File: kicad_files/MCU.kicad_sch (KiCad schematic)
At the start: 24 parts, among them SW1 SW_Push, SW2 SW_Push, U1 STM32F407VGTx, Y1 LFXTAL036869Reel 8MHz Crystal

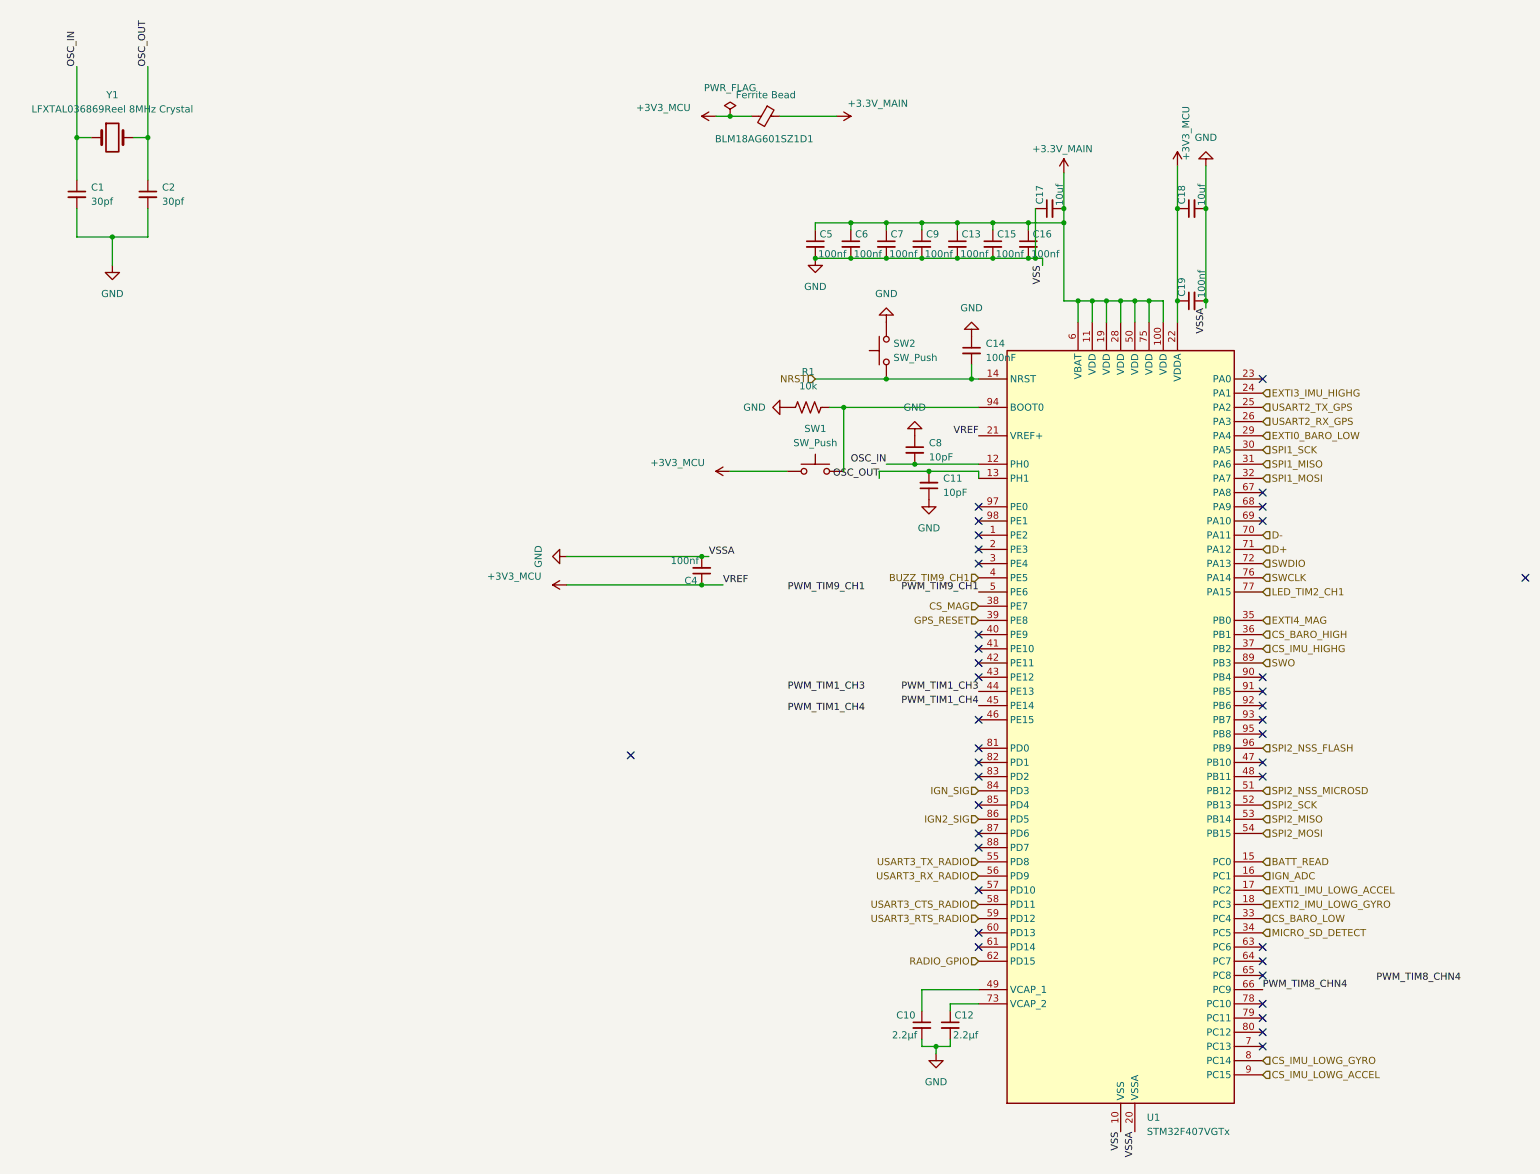
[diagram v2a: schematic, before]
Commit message: add dedicated power switching
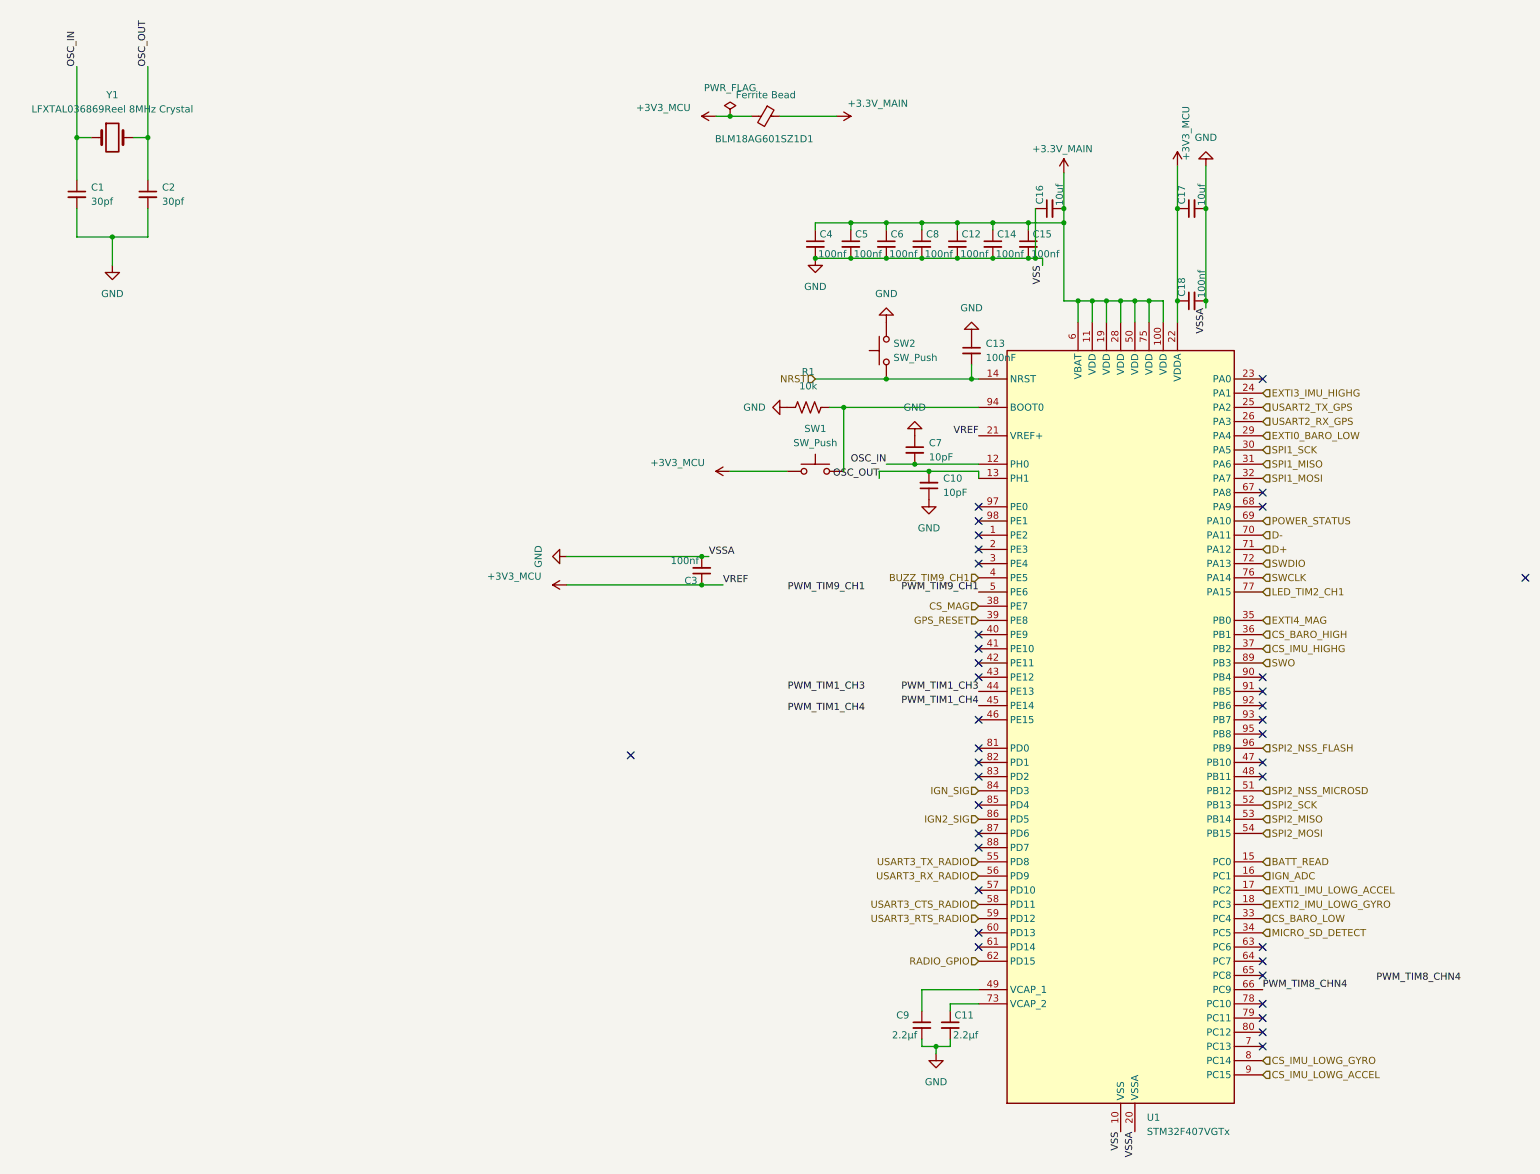
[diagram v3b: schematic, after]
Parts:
- renumbered C11 to C10, C12 to C11, C13 to C12, C14 to C13, C15 to C14, C16 to C15, C17 to C16, C18 to C17, C19 to C18, C4 to C3, C5 to C4, C6 to C5, C7 to C6, C8 to C7, C9 to C8, C10 to C9
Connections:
- net POWER_STATUS: now reaches U1.69 (PA10)
- no-connect marks 39 -> 38
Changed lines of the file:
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@@
 	)
 	(no_connect
-		(at 250.19 119.38)
-	)
-	(no_connect
 		(at 250.19 157.48)
 	)
@@
 		)
 	)
+	(hierarchical_label "POWER_STATUS"
+		(shape input)
+		(at 250.19 119.38 0)
+		(effects
+			(font
+				(size 1.27 1.27)
+			)
+			(justify left)
+		)
+	)
 	(hierarchical_label "CS_IMU_LOWG_GYRO"
 		(shape input)
@@
 		(in_pos_files yes)
 		(dnp no)
-		(property "Reference" "C16"
+		(property "Reference" "C15"
 			(at 209.042 68.072 0)
 			(show_name no)
@@
 			(project "versorlite"
 				(path "/1a230af0-0a74-48f7-8607-b087121dda49/a6e36be3-aff5-4566-a903-d81edfd88a96"
-					(reference "C16")
+					(reference "C15")
 					(unit 1)
 				)
@@
 		(dnp no)
 		(fields_autoplaced yes)
-		(property "Reference" "#PWR05"
+		(property "Reference" "#PWR06"
 			(at 158.75 99.06 0)
 			(hide yes)
@@
 			(project "versorlite"
 				(path "/1a230af0-0a74-48f7-8607-b087121dda49/a6e36be3-aff5-4566-a903-d81edfd88a96"
-					(reference "#PWR05")
+					(reference "#PWR06")
 					(unit 1)
 				)
@@
 		(in_pos_files yes)
 		(dnp no)
-		(property "Reference" "C9"
+		(property "Reference" "C8"
 			(at 189.992 68.072 0)
 			(show_name no)
@@
 			(project "versorlite"
 				(path "/1a230af0-0a74-48f7-8607-b087121dda49/a6e36be3-aff5-4566-a903-d81edfd88a96"
-					(reference "C9")
+					(reference "C8")
 					(unit 1)
 				)
@@
 		(in_pos_files yes)
 		(dnp no)
-		(property "Reference" "#PWR014"
+		(property "Reference" "#PWR015"
 			(at 234.95 59.69 0)
 			(hide yes)
@@
 			(project "versorlite"
 				(path "/1a230af0-0a74-48f7-8607-b087121dda49/a6e36be3-aff5-4566-a903-d81edfd88a96"
-					(reference "#PWR014")
+					(reference "#PWR015")
 					(unit 1)
 				)
@@
 		(dnp no)
 		(fields_autoplaced yes)
-		(property "Reference" "#PWR012"
+		(property "Reference" "#PWR013"
 			(at 198.12 80.01 0)
 			(hide yes)
@@
 			(project "versorlite"
 				(path "/1a230af0-0a74-48f7-8607-b087121dda49/a6e36be3-aff5-4566-a903-d81edfd88a96"
-					(reference "#PWR012")
+					(reference "#PWR013")
 					(unit 1)
 				)
@@
 		(dnp no)
 		(fields_autoplaced yes)
-		(property "Reference" "C8"
+		(property "Reference" "C7"
 			(at 190.5 105.4162 0)
 			(show_name no)
@@
 			(project "versorlite"
 				(path "/1a230af0-0a74-48f7-8607-b087121dda49/a6e36be3-aff5-4566-a903-d81edfd88a96"
-					(reference "C8")
+					(reference "C7")
 					(unit 1)
 				)
@@
 		(in_pos_files yes)
 		(dnp no)
-		(property "Reference" "C5"
+		(property "Reference" "C4"
 			(at 170.942 68.072 0)
 			(show_name no)
@@
 			(project "versorlite"
 				(path "/1a230af0-0a74-48f7-8607-b087121dda49/a6e36be3-aff5-4566-a903-d81edfd88a96"
-					(reference "C5")
+					(reference "C4")
 					(unit 1)
 				)
@@
 		(dnp no)
 		(fields_autoplaced yes)
-		(property "Reference" "C11"
+		(property "Reference" "C10"
 			(at 193.04 111.7535 0)
 			(show_name no)
@@
 			(project "versorlite"
 				(path "/1a230af0-0a74-48f7-8607-b087121dda49/a6e36be3-aff5-4566-a903-d81edfd88a96"
-					(reference "C11")
+					(reference "C10")
 					(unit 1)
 				)
@@
 		(in_pos_files yes)
 		(dnp no)
-		(property "Reference" "C4"
+		(property "Reference" "C3"
 			(at 149.098 130.048 0)
 			(show_name no)
@@
 			(project "versorlite"
 				(path "/1a230af0-0a74-48f7-8607-b087121dda49/a6e36be3-aff5-4566-a903-d81edfd88a96"
-					(reference "C4")
+					(reference "C3")
 					(unit 1)
 				)
@@
 		(in_pos_files yes)
 		(dnp no)
-		(property "Reference" "C7"
+		(property "Reference" "C6"
 			(at 183.642 68.072 0)
 			(show_name no)
@@
 			(project "versorlite"
 				(path "/1a230af0-0a74-48f7-8607-b087121dda49/a6e36be3-aff5-4566-a903-d81edfd88a96"
-					(reference "C7")
+					(reference "C6")
 					(unit 1)
 				)
@@
 		(in_pos_files yes)
 		(dnp no)
-		(property "Reference" "C10"
+		(property "Reference" "C9"
 			(at 184.658 207.772 0)
 			(show_name no)
@@
 			(project "versorlite"
 				(path "/1a230af0-0a74-48f7-8607-b087121dda49/a6e36be3-aff5-4566-a903-d81edfd88a96"
-					(reference "C10")
+					(reference "C9")
 					(unit 1)
 				)
@@
 		(in_pos_files yes)
 		(dnp no)
-		(property "Reference" "#PWR053"
+		(property "Reference" "#PWR05"
 			(at 158.75 110.49 0)
 			(hide yes)
@@
 			(project "versorlite"
 				(path "/1a230af0-0a74-48f7-8607-b087121dda49/a6e36be3-aff5-4566-a903-d81edfd88a96"
-					(reference "#PWR053")
+					(reference "#PWR05")
 					(unit 1)
 				)
@@
 		(dnp no)
 		(fields_autoplaced yes)
-		(property "Reference" "#PWR015"
+		(property "Reference" "#PWR016"
 			(at 240.03 49.53 0)
 			(hide yes)
@@
 			(project "versorlite"
 				(path "/1a230af0-0a74-48f7-8607-b087121dda49/a6e36be3-aff5-4566-a903-d81edfd88a96"
-					(reference "#PWR015")
+					(reference "#PWR016")
 					(unit 1)
 				)
@@
 		(in_pos_files yes)
 		(dnp no)
-		(property "Reference" "C18"
+		(property "Reference" "C17"
 			(at 235.712 62.738 0)
 			(show_name no)
@@
 			(project "versorlite"
 				(path "/1a230af0-0a74-48f7-8607-b087121dda49/a6e36be3-aff5-4566-a903-d81edfd88a96"
-					(reference "C18")
+					(reference "C17")
 					(unit 1)
 				)
@@
 		(dnp no)
 		(fields_autoplaced yes)
-		(property "Reference" "#PWR09"
+		(property "Reference" "#PWR010"
 			(at 187.96 97.79 0)
 			(hide yes)
@@
 			(project "versorlite"
 				(path "/1a230af0-0a74-48f7-8607-b087121dda49/a6e36be3-aff5-4566-a903-d81edfd88a96"
-					(reference "#PWR09")
+					(reference "#PWR010")
 					(unit 1)
 				)
@@
 		(in_pos_files yes)
 		(dnp no)
-		(property "Reference" "C19"
+		(property "Reference" "C18"
 			(at 235.712 79.248 0)
 			(show_name no)
@@
 			(project "versorlite"
 				(path "/1a230af0-0a74-48f7-8607-b087121dda49/a6e36be3-aff5-4566-a903-d81edfd88a96"
-					(reference "C19")
+					(reference "C18")
 					(unit 1)
 				)
@@
 		(in_pos_files yes)
 		(dnp no)
-		(property "Reference" "#PWR07"
+		(property "Reference" "#PWR08"
 			(at 170.18 46.99 0)
 			(hide yes)
@@
 			(project "versorlite"
 				(path "/1a230af0-0a74-48f7-8607-b087121dda49/a6e36be3-aff5-4566-a903-d81edfd88a96"
-					(reference "#PWR07")
+					(reference "#PWR08")
 					(unit 1)
 				)
@@
 		(in_pos_files yes)
 		(dnp no)
-		(property "Reference" "C17"
+		(property "Reference" "C16"
 			(at 210.312 62.738 0)
 			(show_name no)
@@
 			(project "versorlite"
 				(path "/1a230af0-0a74-48f7-8607-b087121dda49/a6e36be3-aff5-4566-a903-d81edfd88a96"
-					(reference "C17")
+					(reference "C16")
 					(unit 1)
 				)
@@
 		(in_pos_files yes)
 		(dnp no)
-		(property "Reference" "#PWR013"
+		(property "Reference" "#PWR014"
 			(at 214.63 60.96 0)
 			(hide yes)
@@
 			(project "versorlite"
 				(path "/1a230af0-0a74-48f7-8607-b087121dda49/a6e36be3-aff5-4566-a903-d81edfd88a96"
-					(reference "#PWR013")
+					(reference "#PWR014")
 					(unit 1)
 				)
@@
 		(in_pos_files yes)
 		(dnp no)
-		(property "Reference" "C15"
+		(property "Reference" "C14"
 			(at 202.692 68.072 0)
 			(show_name no)
@@
 			(project "versorlite"
 				(path "/1a230af0-0a74-48f7-8607-b087121dda49/a6e36be3-aff5-4566-a903-d81edfd88a96"
-					(reference "C15")
+					(reference "C14")
 					(unit 1)
 				)
@@
 		(in_pos_files yes)
 		(dnp no)
-		(property "Reference" "C12"
+		(property "Reference" "C11"
 			(at 195.072 207.772 0)
 			(show_name no)
@@
 			(project "versorlite"
 				(path "/1a230af0-0a74-48f7-8607-b087121dda49/a6e36be3-aff5-4566-a903-d81edfd88a96"
-					(reference "C12")
+					(reference "C11")
 					(unit 1)
 				)
@@
 		(dnp no)
 		(fields_autoplaced yes)
-		(property "Reference" "#PWR06"
+		(property "Reference" "#PWR07"
 			(at 170.18 78.74 0)
 			(hide yes)
@@
 			(project "versorlite"
 				(path "/1a230af0-0a74-48f7-8607-b087121dda49/a6e36be3-aff5-4566-a903-d81edfd88a96"
-					(reference "#PWR06")
+					(reference "#PWR07")
 					(unit 1)
 				)
@@
 		(in_pos_files yes)
 		(dnp no)
-		(property "Reference" "C13"
+		(property "Reference" "C12"
 			(at 196.342 68.072 0)
 			(show_name no)
@@
 			(project "versorlite"
 				(path "/1a230af0-0a74-48f7-8607-b087121dda49/a6e36be3-aff5-4566-a903-d81edfd88a96"
-					(reference "C13")
+					(reference "C12")
 					(unit 1)
 				)
@@
 		(dnp no)
 		(fields_autoplaced yes)
-		(property "Reference" "#PWR011"
+		(property "Reference" "#PWR012"
 			(at 191.77 220.98 0)
 			(hide yes)
@@
 			(project "versorlite"
 				(path "/1a230af0-0a74-48f7-8607-b087121dda49/a6e36be3-aff5-4566-a903-d81edfd88a96"
-					(reference "#PWR011")
+					(reference "#PWR012")
 					(unit 1)
 				)
@@
 		(dnp no)
 		(fields_autoplaced yes)
-		(property "Reference" "C14"
+		(property "Reference" "C13"
 			(at 200.66 87.6362 0)
 			(show_name no)
@@
 			(project "versorlite"
 				(path "/1a230af0-0a74-48f7-8607-b087121dda49/a6e36be3-aff5-4566-a903-d81edfd88a96"
-					(reference "C14")
+					(reference "C13")
 					(unit 1)
 				)
@@
 		(dnp no)
 		(fields_autoplaced yes)
-		(property "Reference" "#PWR010"
+		(property "Reference" "#PWR011"
 			(at 190.5 121.92 0)
 			(hide yes)
@@
 			(project "versorlite"
 				(path "/1a230af0-0a74-48f7-8607-b087121dda49/a6e36be3-aff5-4566-a903-d81edfd88a96"
-					(reference "#PWR010")
+					(reference "#PWR011")
 					(unit 1)
 				)
@@
 		(in_pos_files yes)
 		(dnp no)
-		(property "Reference" "C6"
+		(property "Reference" "C5"
 			(at 177.292 68.072 0)
 			(show_name no)
@@
 			(project "versorlite"
 				(path "/1a230af0-0a74-48f7-8607-b087121dda49/a6e36be3-aff5-4566-a903-d81edfd88a96"
-					(reference "C6")
+					(reference "C5")
 					(unit 1)
 				)
@@
 		(dnp no)
 		(fields_autoplaced yes)
-		(property "Reference" "#PWR08"
+		(property "Reference" "#PWR09"
 			(at 182.88 77.47 0)
 			(hide yes)
@@
 			(project "versorlite"
 				(path "/1a230af0-0a74-48f7-8607-b087121dda49/a6e36be3-aff5-4566-a903-d81edfd88a96"
-					(reference "#PWR08")
+					(reference "#PWR09")
 					(unit 1)
 				)

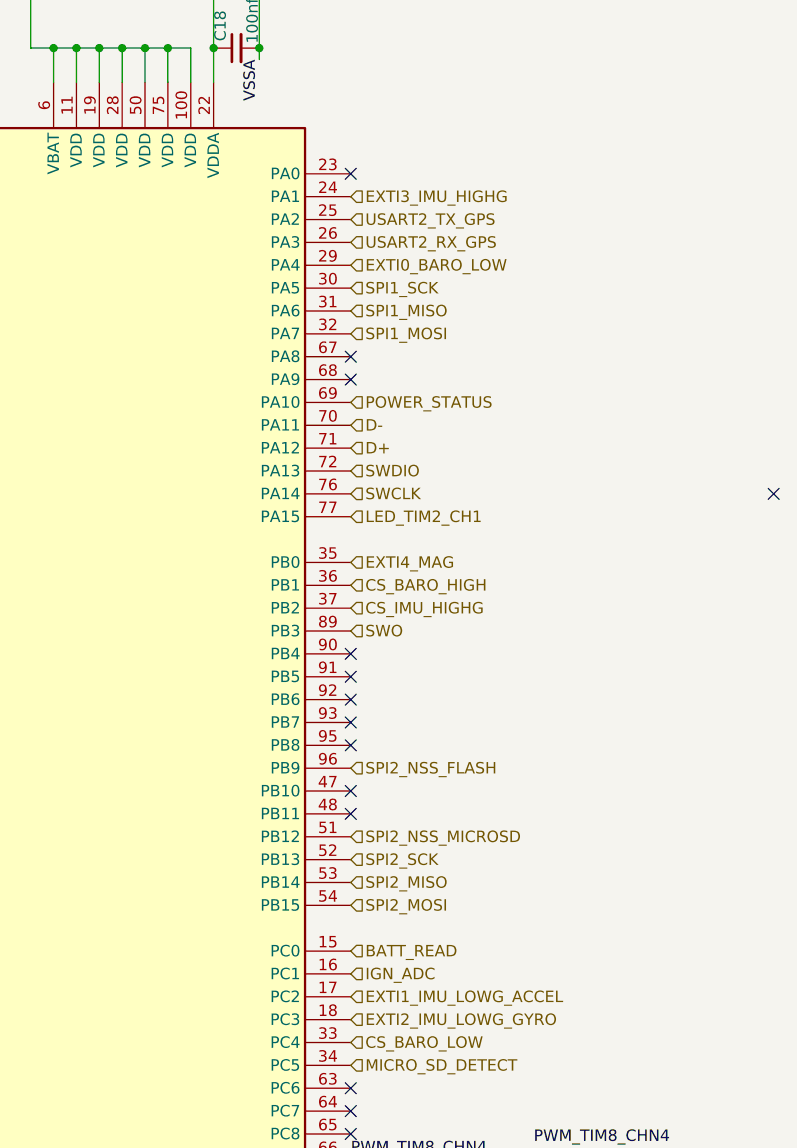
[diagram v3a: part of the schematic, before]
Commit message: add ign_adc2
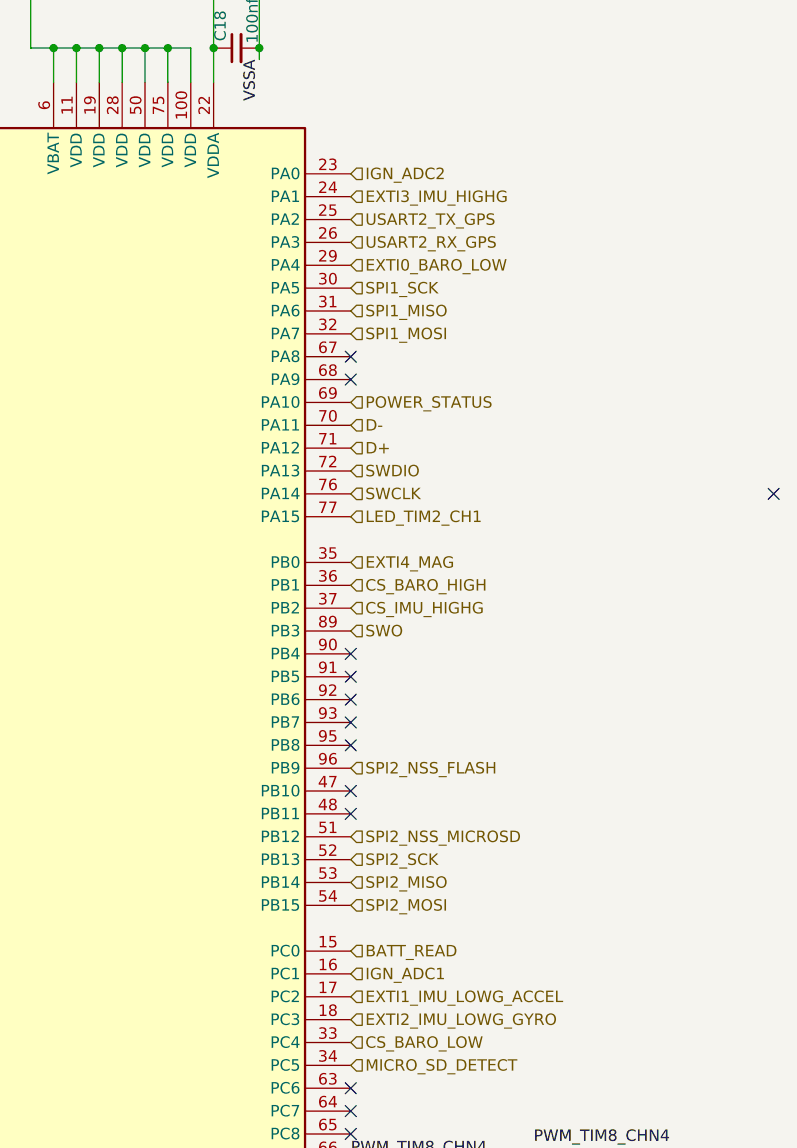
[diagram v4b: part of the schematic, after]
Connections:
- net IGN_ADC2: now reaches U1.23 (PA0)
- net IGN_ADC renamed IGN_ADC1
- no-connect marks 38 -> 37
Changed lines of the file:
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@@
-	)
-	(no_connect
-		(at 250.19 93.98)
 	)
 	(no_connect
@@
 		)
 	)
+	(hierarchical_label "IGN_ADC2"
+		(shape input)
+		(at 250.19 93.98 0)
+		(effects
+			(font
+				(size 1.27 1.27)
+			)
+			(justify left)
+		)
+	)
 	(hierarchical_label "BATT_READ"
 		(shape input)
@@
 		)
 	)
-	(hierarchical_label "IGN_ADC"
+	(hierarchical_label "IGN_ADC1"
 		(shape input)
 		(at 250.19 182.88 0)
